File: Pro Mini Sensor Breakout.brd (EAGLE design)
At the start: 35.6 x 40.6 mm, 19 parts, among them J1 22-27-2021-02, J10 22-27-2021-02, J11 22-27-2021-02, J12 22-27-2021-02, J2 22-27-2041-04, J3 22-27-2041-04, J4 22-27-2031-03, J5 22-27-2041-04, J6 22-27-2041-04, J7 22-27-2031-03, J8 22-27-2021-02, J9 22-27-2021-02, U1 ARDUINO_PRO_MINI

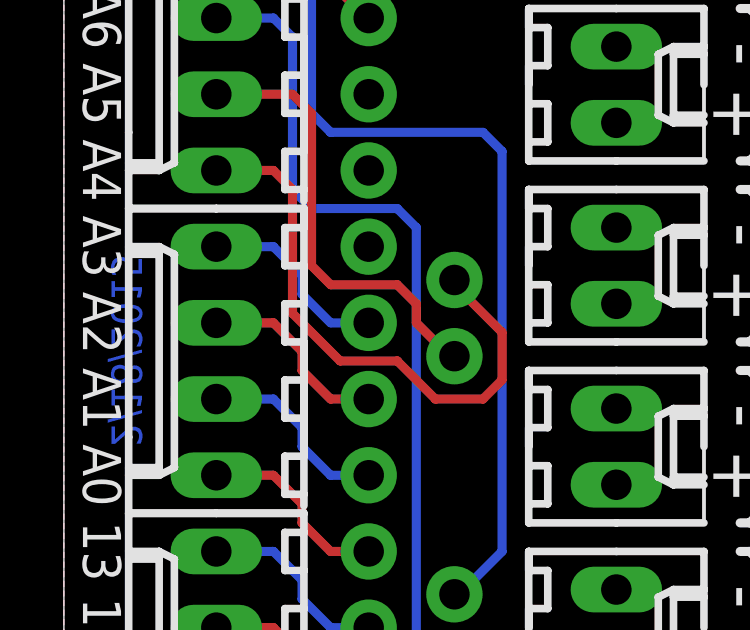
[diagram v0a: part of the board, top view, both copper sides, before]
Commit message: Corrected mis-wire of A4 & A5.
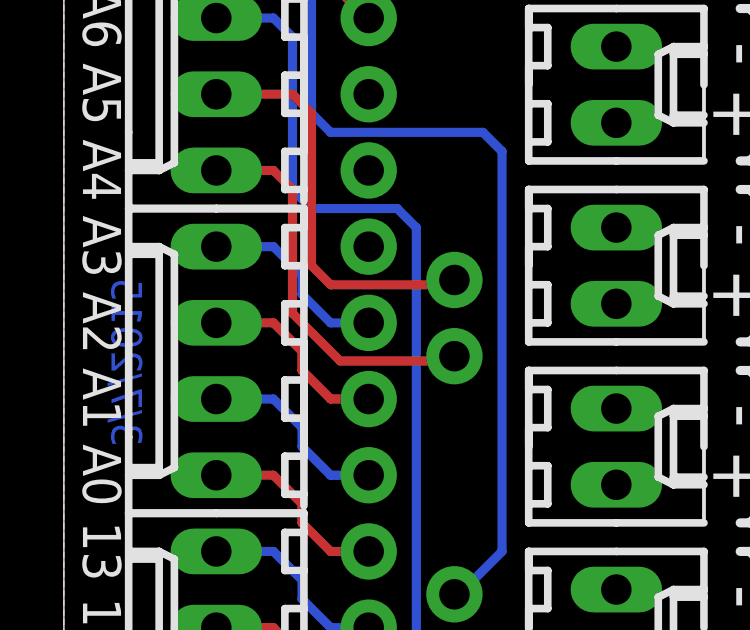
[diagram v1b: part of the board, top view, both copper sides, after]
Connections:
- removed net N$3: J2.4, U1.A5
- new net N$1: J2.4, U1.A4
- net N$2: now also U1.A5; no longer U1.A4
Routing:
- net N$3: track 19.2 -> 0.00 mm
- net N$1: track 0.00 -> 13.0 mm
- net N$2: track 15.0 -> 13.5 mm
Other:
- board text added: "3/7/2015"
- board text added: "Arduino Pro Mini Sensor Breakout v2"
- board text removed: "2/18/2015"
- board text removed: "Arduino Pro Mini Sensor Breakout v1"
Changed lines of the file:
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@@
 <text x="7.3025" y="1.27" size="1.016" layer="22" font="vector" rot="MR90">(C) 2015 D. Wassenberg</text>
 <text x="7.3025" y="23.8125" size="1.016" layer="22" font="vector" rot="MR90">CC BY-SA 4.0</text>
-<text x="27.305" y="2.54" size="1.016" layer="22" font="vector" rot="SMR90">Arduino Pro Mini Sensor Breakout v1</text>
+<text x="27.305" y="2.54" size="1.016" layer="22" font="vector" rot="SMR90">Arduino Pro Mini Sensor Breakout v2</text>
 <text x="23.1775" y="26.3525" size="1.778" layer="21" font="vector" rot="R90">+</text>
 <text x="23.1775" y="20.32" size="1.778" layer="21" font="vector" rot="R90">+</text>
@@
 <text x="34.29" y="30.7975" size="1.27" layer="21" font="vector" rot="SR90" align="center">RX</text>
 <text x="34.29" y="33.3375" size="1.27" layer="21" font="vector" rot="SR90" align="center">TX</text>
-<text x="1.5875" y="16.1925" size="1.016" layer="16" font="vector" ratio="15" rot="MR90">2/18/2015</text>
+<text x="1.5875" y="16.1925" size="1.016" layer="16" font="vector" ratio="15" rot="MR90">3/7/2015</text>
 <text x="21.59" y="37.1475" size="0.8636" layer="21" font="vector" ratio="10" rot="R90">-</text>
 <text x="13.6525" y="40.3225" size="0.8636" layer="51" font="vector" ratio="10" rot="R270">+3.3-12V</text>
@@
 <contactref element="J12" pad="1"/>
 </signal>
-<signal name="N$2">
-<contactref element="J2" pad="3"/>
-<contactref element="U1" pad="A4"/>
-<wire x1="5.08" y1="27.94" x2="7.62" y2="27.94" width="0.3048" layer="1"/>
-<wire x1="7.62" y1="27.94" x2="8.255" y2="27.305" width="0.3048" layer="1"/>
-<wire x1="8.255" y1="27.305" x2="8.255" y2="22.225" width="0.3048" layer="1"/>
-<wire x1="8.255" y1="22.225" x2="8.89" y2="21.59" width="0.3048" layer="1"/>
-<wire x1="8.89" y1="21.59" x2="11.1125" y2="21.59" width="0.3048" layer="1"/>
-<wire x1="11.1125" y1="21.59" x2="11.7475" y2="20.955" width="0.3048" layer="1"/>
-<wire x1="11.7475" y1="20.955" x2="11.7475" y2="20.32" width="0.3048" layer="1"/>
-<wire x1="11.7475" y1="20.32" x2="13.0175" y2="19.05" width="0.3048" layer="1"/>
-<wire x1="13.0175" y1="19.05" x2="13.0175" y2="19.20875" width="0" layer="19" extent="1-1"/>
-</signal>
-<signal name="N$3">
-<contactref element="U1" pad="A5"/>
-<contactref element="J2" pad="4"/>
-<wire x1="5.08" y1="25.4" x2="6.985" y2="25.4" width="0.3048" layer="1"/>
-<wire x1="6.985" y1="25.4" x2="7.62" y2="24.765" width="0.3048" layer="1"/>
-<wire x1="7.62" y1="20.6375" x2="9.2075" y2="19.05" width="0.3048" layer="1"/>
-<wire x1="9.2075" y1="19.05" x2="11.1125" y2="19.05" width="0.3048" layer="1"/>
-<wire x1="11.1125" y1="19.05" x2="12.3825" y2="17.78" width="0.3048" layer="1"/>
-<wire x1="12.3825" y1="17.78" x2="13.97" y2="17.78" width="0.3048" layer="1"/>
-<wire x1="13.97" y1="17.78" x2="14.605" y2="18.415" width="0.3048" layer="1"/>
-<wire x1="14.605" y1="18.415" x2="14.605" y2="20.0025" width="0.3048" layer="1"/>
-<wire x1="14.605" y1="20.0025" x2="13.0175" y2="21.59" width="0.3048" layer="1"/>
-<wire x1="7.62" y1="24.765" x2="7.62" y2="20.6375" width="0.3048" layer="1"/>
-<wire x1="13.0175" y1="21.59" x2="13.0175" y2="21.74875" width="0" layer="19" extent="1-1"/>
-</signal>
 <signal name="N$4">
 <contactref element="J2" pad="1"/>
@@
 <wire x1="11.43" y1="1.27" x2="10.16" y2="2.54" width="0.3048" layer="1"/>
 </signal>
+<signal name="N$1">
+<contactref element="J2" pad="4"/>
+<contactref element="U1" pad="A4"/>
+<wire x1="5.08" y1="25.4" x2="6.985" y2="25.4" width="0.3048" layer="1"/>
+<wire x1="6.985" y1="25.4" x2="7.62" y2="24.765" width="0.3048" layer="1"/>
+<wire x1="7.62" y1="24.765" x2="7.62" y2="20.6375" width="0.3048" layer="1"/>
+<wire x1="7.62" y1="20.6375" x2="9.2075" y2="19.05" width="0.3048" layer="1"/>
+<wire x1="9.2075" y1="19.05" x2="13.0175" y2="19.05" width="0.3048" layer="1"/>
+<wire x1="13.0175" y1="19.05" x2="13.0175" y2="19.20875" width="0" layer="19" extent="1-1"/>
+</signal>
+<signal name="N$2">
+<contactref element="U1" pad="A5"/>
+<contactref element="J2" pad="3"/>
+<wire x1="5.08" y1="27.94" x2="7.62" y2="27.94" width="0.3048" layer="1"/>
+<wire x1="7.62" y1="27.94" x2="8.255" y2="27.305" width="0.3048" layer="1"/>
+<wire x1="8.255" y1="27.305" x2="8.255" y2="22.225" width="0.3048" layer="1"/>
+<wire x1="8.255" y1="22.225" x2="8.89" y2="21.59" width="0.3048" layer="1"/>
+<wire x1="8.89" y1="21.59" x2="13.0175" y2="21.59" width="0.3048" layer="1"/>
+<wire x1="13.0175" y1="21.59" x2="13.0175" y2="21.74875" width="0" layer="19" extent="1-1"/>
+</signal>
 </signals>
